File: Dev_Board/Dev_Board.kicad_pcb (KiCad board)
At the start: 2 copper layers, 43.6 x 63.2 mm, 55 parts, among them J1 Conn_01x04, J2 Conn_01x04, J3 Conn_01x04, J4 Conn_01x04, J5 Conn_01x04, J6 Conn_01x04, J7 Conn_01x04, J8 Conn_01x04

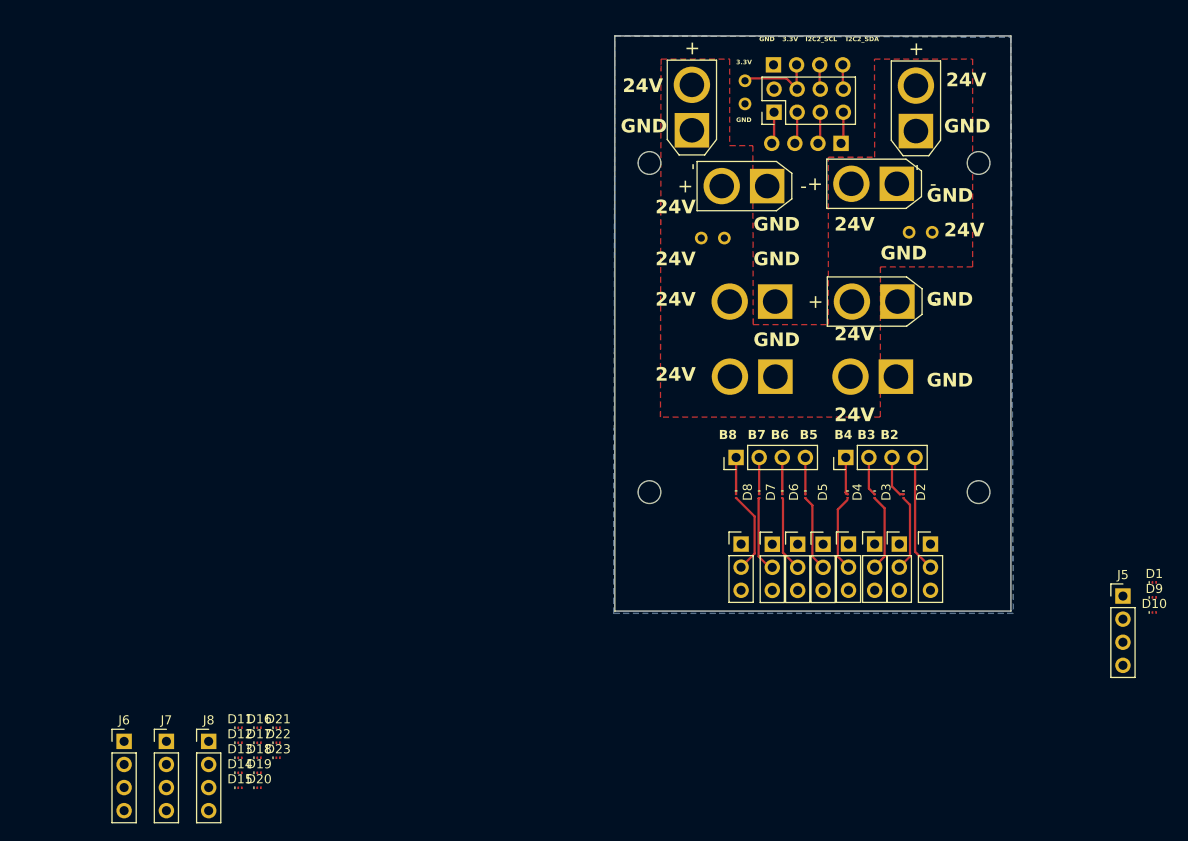
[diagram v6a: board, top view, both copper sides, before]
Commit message: forgot to add mounting holes
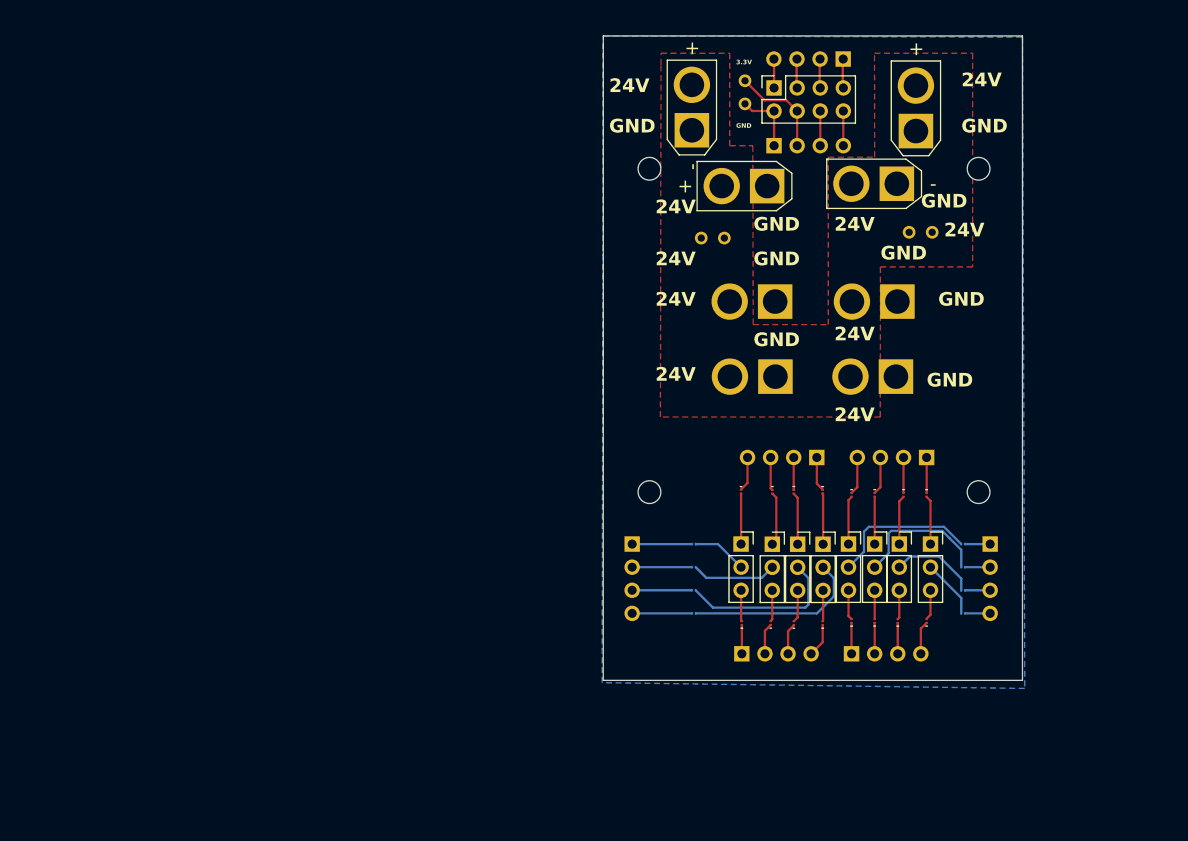
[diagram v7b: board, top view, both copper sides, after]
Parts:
- removed the REF** at (188.6, 45.7)
- removed the REF** at (224.8, 45.7)
- added D24: D, Diode_SMD:Nexperia_DSN0603-2_0.6x0.3mm_P0.4mm, B.Cu at (223.1, 95.2)
- added REF**: MountingHole_2.5mm, MountingHole:MountingHole_2.5mm, F.Cu at (224.8, 46.4)
- added REF**: MountingHole_2.5mm, MountingHole:MountingHole_2.5mm, F.Cu at (188.6, 46.4)
- D2, D3, D4, D5, D6, D7, D8, J3, J4, J5, J6, J7, J8, Out_Port8: moved to B.Cu
- DBUS1, PWM_R1, PWM_R2, PWM_R3, PWM_R4, PWM_R5, PWM_R6, PWM_R7: footprint Connector_PinHeader_2.54mm:PinHeader_1x03_P2.54mm_Vertical -> Connector_PinSocket_2.54mm:PinSocket_1x03_P2.54mm_Vertical
- IO_Port1: footprint Connector_PinHeader_2.54mm:PinHeader_2x04_P2.54mm_Vertical -> Connector_PinSocket_2.54mm:PinSocket_2x04_P2.54mm_Vertical
- moved J6 82.3 mm to (207.0, 78.1), turned to 90 degrees
- moved J7 76.0 mm to (210.8, 99.7), turned to -90 degrees
- moved D19 75.3 mm to (219.1, 96.1), turned to 90 degrees
- moved D11 72.0 mm to (210.8, 82.2), turned to -90 degrees
- moved D18 71.8 mm to (215.9, 96.1), turned to 90 degrees
- moved D12 69.8 mm to (207.6, 81.9), turned to -90 degrees
- moved D17 69.0 mm to (213.4, 96.1), turned to 90 degrees
- moved D13 67.6 mm to (204.5, 81.9), turned to -90 degrees
- moved D16 66.2 mm to (210.8, 96.1), turned to 90 degrees
- moved D14 66.2 mm to (202.1, 81.9), turned to -90 degrees
- moved D15 64.0 mm to (198.7, 81.9), turned to -90 degrees
- moved D23 61.7 mm to (207.6, 96.3), turned to 90 degrees
- moved J8 59.4 mm to (198.8, 99.7), turned to -90 degrees
- moved D22 58.2 mm to (204.5, 96.3), turned to 90 degrees
- moved D20 56.1 mm to (198.8, 96.3), turned to 90 degrees
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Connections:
- D8 pad 1: Net-(D21-A) -> Net-(D8-K)
- J3 pad 1: Net-(D21-A) -> Net-(D8-K)
- J4 pad 4: /B1 (5V) -> Net-(D24-K)
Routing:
- net /B5: track 8.39 -> 19.7 mm
- net /B6: track 8.29 -> 17.9 mm
- net /B4: track 8.35 -> 16.3 mm
- net GND: track 1.75 -> 8.58 mm
- net /B3: track 8.51 -> 15.2 mm
- net Net-(D8-K): track 0.00 -> 6.53 mm
- net /B1 (5V): track 12.8 -> 6.48 mm
- net Net-(D14-A): track 0.00 -> 5.93 mm
- net /A6: track 0.00 -> 5.70 mm
- net /A5: track 0.00 -> 5.59 mm
- net Net-(D15-A): track 0.00 -> 5.56 mm
- net /A2: track 0.00 -> 5.37 mm
- net /A1 (GND): track 0.00 -> 5.35 mm
- net /A4: track 0.00 -> 5.31 mm
- net /A3: track 0.00 -> 5.17 mm
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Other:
- board size 43.6 x 63.2 mm -> 46.1 x 70.9 mm
- board text added: "D1"
- board text added: "SCL"
- board text added: "SDA"
- board text removed: "B2"
- board text removed: "B3"
- board text removed: "B4"
- board text removed: "B5"
- board text removed: "B6"
- board text removed: "B7"
- board text removed: "B8"
- board text removed: "I2C2_SCL"
- board text removed: "I2C2_SDA"

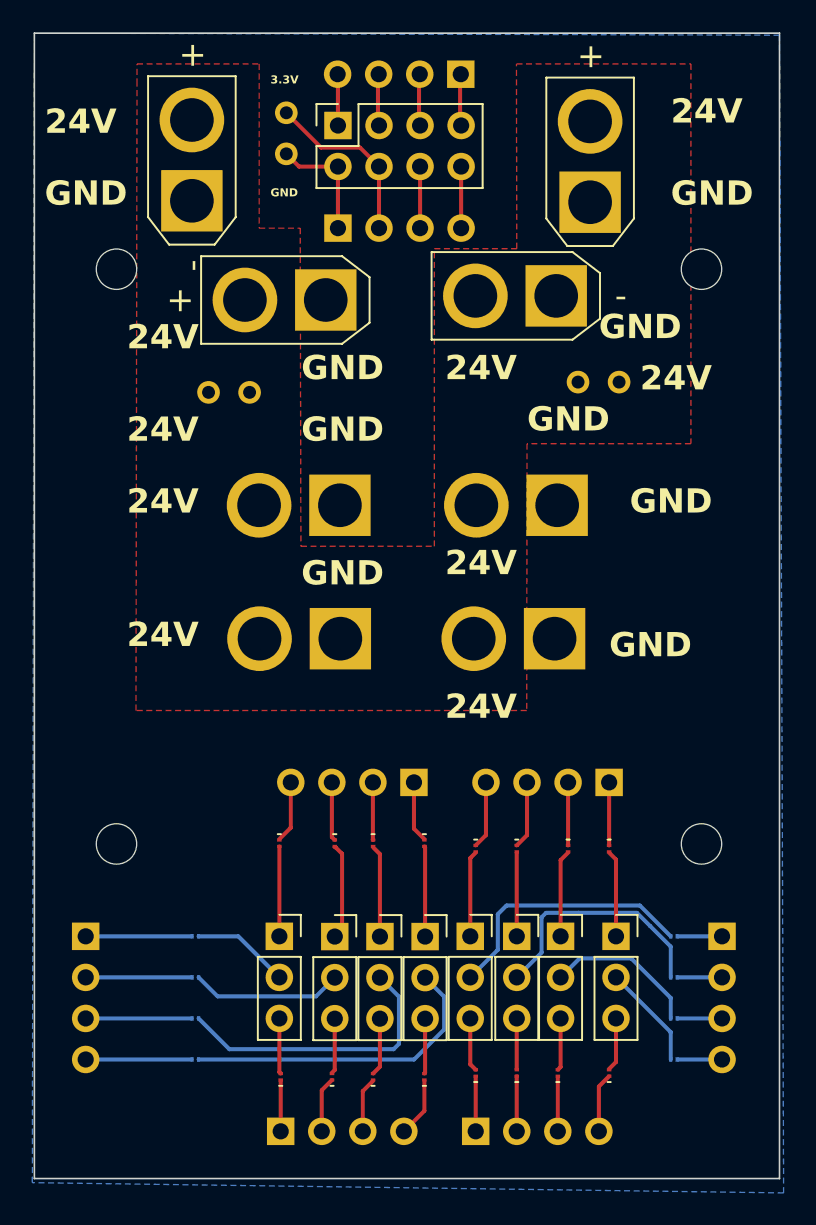
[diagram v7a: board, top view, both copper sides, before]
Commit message: fixed the tracks and pin headers and I only added diodes to the 3.3V pins
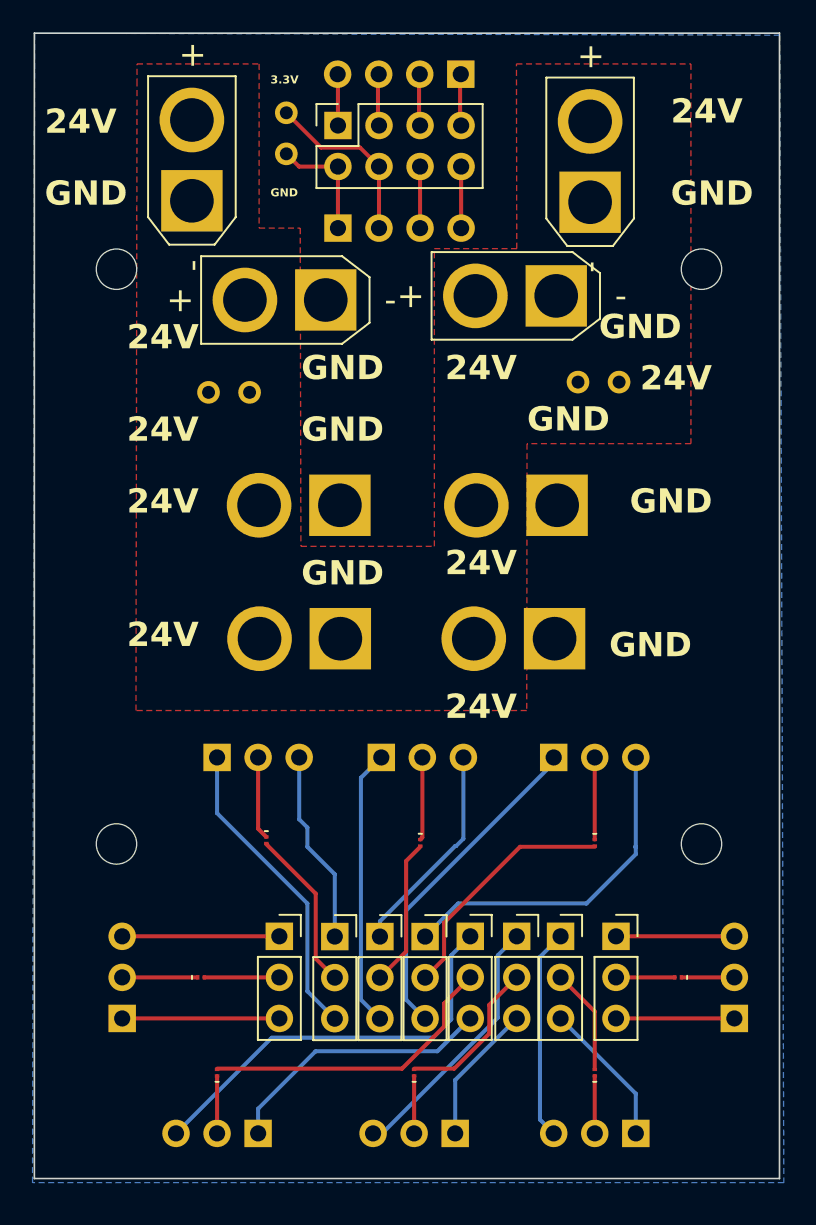
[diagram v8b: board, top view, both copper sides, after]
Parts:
- removed D10, D12, D13, D15, D16, D18, D19, D2, D21, D22, D24, D3, D5, D6, D8, D9: D, Diode_SMD:Nexperia_DSN0603-2_0.6x0.3mm_P0.4mm
- removed J3, J4, J5, J6, J7, J8: Conn_01x04, Connector_PinHeader_2.54mm:PinHeader_1x04_P2.54mm_Vertical
- removed REF** (x4): MountingHole_2.5mm, MountingHole:MountingHole_2.5mm
- added H1: MountingHole, MountingHole:MountingHole_2.5mm, F.Cu at (188.6, 46.4)
- added H2: MountingHole, MountingHole:MountingHole_2.5mm, F.Cu at (188.6, 81.9)
- added H3: MountingHole, MountingHole:MountingHole_2.5mm, F.Cu at (224.8, 81.9)
- added H4: MountingHole, MountingHole:MountingHole_2.5mm, F.Cu at (224.8, 46.4)
- added PWM_R10: Conn_01x03, Connector_PinHeader_2.54mm:PinHeader_1x03_P2.54mm_Vertical, B.Cu at (209.6, 99.8)
- added PWM_R11: Conn_01x03, Connector_PinHeader_2.54mm:PinHeader_1x03_P2.54mm_Vertical, B.Cu at (197.4, 99.8)
- added PWM_R12: Conn_01x03, Connector_PinHeader_2.54mm:PinHeader_1x03_P2.54mm_Vertical, B.Cu at (215.6, 76.6)
- added PWM_R13: Conn_01x03, Connector_PinHeader_2.54mm:PinHeader_1x03_P2.54mm_Vertical, B.Cu at (205.0, 76.6)
- added PWM_R14: Conn_01x03, Connector_PinHeader_2.54mm:PinHeader_1x03_P2.54mm_Vertical, B.Cu at (194.8, 76.6)
- added PWM_R15: Conn_01x03, Connector_PinHeader_2.54mm:PinHeader_1x03_P2.54mm_Vertical, B.Cu at (188.9, 92.7)
- added PWM_R8: Conn_01x03, Connector_PinHeader_2.54mm:PinHeader_1x03_P2.54mm_Vertical, B.Cu at (226.8, 92.7)
- added PWM_R9: Conn_01x03, Connector_PinHeader_2.54mm:PinHeader_1x03_P2.54mm_Vertical, B.Cu at (220.7, 99.8)
- D4, D7: moved to F.Cu
- moved D11 21.2 mm to (194.8, 96.1), turned to 90 degrees
- moved D14 16.1 mm to (218.2, 81.8)
- moved D17 15.4 mm to (207.4, 81.8), turned to -90 degrees
- moved D23 15.1 mm to (193.8, 90.2), turned to 0 degrees
- moved D7 14.8 mm to (207.0, 96.1), turned to 90 degrees
- moved D20 14.7 mm to (197.9, 81.7), turned to -90 degrees
- moved D1 12.8 mm to (223.3, 90.2), turned to 180 degrees
- moved D4 9.76 mm to (218.2, 96.1), turned to 90 degrees
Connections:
- D1 pad 2: /A3 -> /B1 (5V)
- D11 pad 2: /A4 -> /B4
- D14 pad 2: Net-(D14-A) -> /B5
- D17 pad 2: /C3 -> /B6
- D20 pad 2: /C8 -> Net-(D20-A)
- D23 pad 2: /C5 -> Net-(D23-A)
- D4 pad 2: /B4 -> Net-(D4-A)
- D7 pad 2: Net-(D7-A) -> /B3
- DBUS1 pad 2: Net-(D8-A) -> Net-(D23-A)
- J1 pad 1: /SPI2_MISO -> unconnected-(J1-Pin_1-Pad1)
- PWM_R1 pad 1: /A1 (GND) -> Net-(PWM_R1-Pin_1)
- PWM_R1 pad 3: /C1 -> Net-(PWM_R1-Pin_3)
- PWM_R2 pad 2: /B2 -> Net-(D4-A)
- PWM_R2 pad 3: /C2 -> Net-(PWM_R2-Pin_3)
- PWM_R6 pad 3: /C6 -> Net-(PWM_R13-Pin_1)
- PWM_R7 pad 1: Net-(D14-A) -> Net-(PWM_R14-Pin_3)
- PWM_R7 pad 2: Net-(D7-A) -> Net-(D20-A)
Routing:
- net /A4: track 5.31 -> 25.6 mm
- net Net-(PWM_R13-Pin_1): track 0.00 -> 17.2 mm
- net /C5: track 3.41 -> 20.4 mm
- net Net-(PWM_R14-Pin_1): track 3.42 -> 19.2 mm
- net /A5: track 5.59 -> 21.2 mm
- net /C4: track 3.31 -> 17.0 mm
- net Net-(PWM_R14-Pin_3): track 0.00 -> 12.0 mm
- net /A3: track 5.17 -> 16.2 mm
- net Net-(D20-A): track 0.00 -> 10.1 mm
- net /B2: track 9.58 -> 0.00 mm
- net Net-(D7-A): track 9.39 -> 0.00 mm
- net Net-(PWM_R2-Pin_3): track 0.00 -> 9.04 mm
- net /B6: track 17.9 -> 9.13 mm
- net /A2: track 5.37 -> 13.1 mm
- net /A6: track 5.70 -> 13.3 mm
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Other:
- board text removed: "D1"
